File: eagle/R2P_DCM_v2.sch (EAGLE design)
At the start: 53 parts, among them Q1 MOSFET-NCHANNELFDD8580, Q2 MOSFET-NCHANNELFDD8580, Q3 MOSFET-NCHANNELFDD8580, Q4 MOSFET-NCHANNELFDD8580, U1 STM32F103CX, U5 LD3985XX, X1 MICROMATCH-4, X2 OSC-XTAL212M_

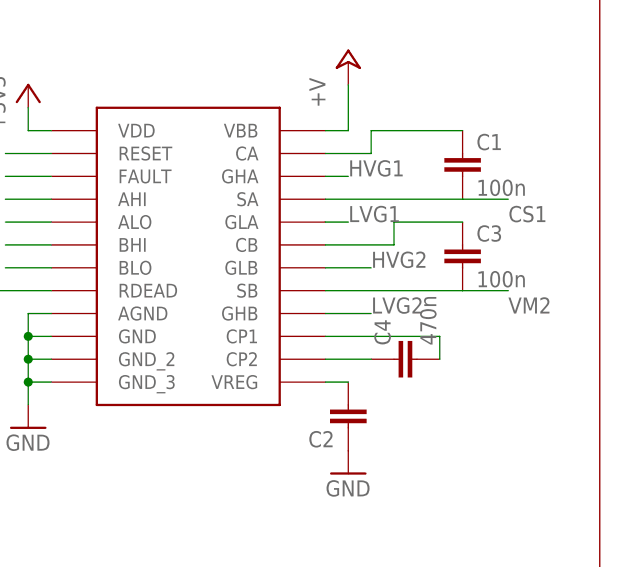
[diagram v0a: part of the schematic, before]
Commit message: Powerpad under A4940
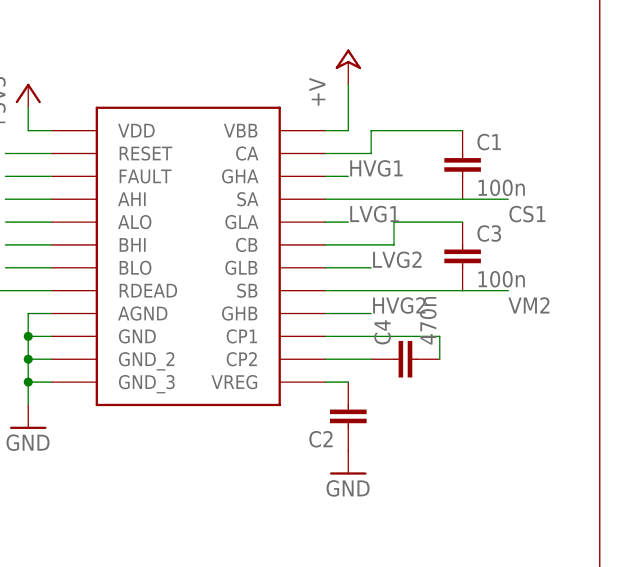
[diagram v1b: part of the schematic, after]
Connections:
- net HVG2: now also U$1.GHB; no longer U$1.GLB
- net LVG2: now also U$1.GLB; no longer U$1.GHB
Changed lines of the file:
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@@
 <net name="HVG2" class="0">
+<segment>
+<wire x1="233.68" y1="226.06" x2="238.76" y2="226.06" width="0.1524" layer="91"/>
+<label x="238.76" y="226.06" size="1.778" layer="95"/>
+<pinref part="R4" gate="G$1" pin="1"/>
+</segment>
+<segment>
+<wire x1="223.52" y1="144.78" x2="228.6" y2="144.78" width="0.1524" layer="91"/>
+<label x="228.6" y="144.78" size="1.778" layer="95"/>
+<pinref part="U$1" gate="G$1" pin="GHB"/>
+</segment>
+</net>
+<net name="LVG2" class="0">
+<segment>
+<wire x1="233.68" y1="205.74" x2="238.76" y2="205.74" width="0.1524" layer="91"/>
+<label x="238.76" y="205.74" size="1.778" layer="95"/>
+<pinref part="R5" gate="G$1" pin="1"/>
+</segment>
 <segment>
 <wire x1="223.52" y1="149.86" x2="228.6" y2="149.86" width="0.1524" layer="91"/>
@@
 <pinref part="U$1" gate="G$1" pin="GLB"/>
 </segment>
-<segment>
-<wire x1="233.68" y1="226.06" x2="238.76" y2="226.06" width="0.1524" layer="91"/>
-<label x="238.76" y="226.06" size="1.778" layer="95"/>
-<pinref part="R4" gate="G$1" pin="1"/>
-</segment>
 </net>
-<net name="LVG2" class="0">
-<segment>
-<wire x1="223.52" y1="144.78" x2="228.6" y2="144.78" width="0.1524" layer="91"/>
-<label x="228.6" y="144.78" size="1.778" layer="95"/>
-<pinref part="U$1" gate="G$1" pin="GHB"/>
-</segment>
-<segment>
-<wire x1="233.68" y1="205.74" x2="238.76" y2="205.74" width="0.1524" layer="91"/>
-<label x="238.76" y="205.74" size="1.778" layer="95"/>
-<pinref part="R5" gate="G$1" pin="1"/>
-</segment>
-</net>
